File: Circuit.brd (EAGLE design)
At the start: 99 x 72.1 mm, 115 parts, among them IC1 LM1117T-3.3-V, P1 RASPI-P1RASPI_REV2_P1, P5 RASPI_P5

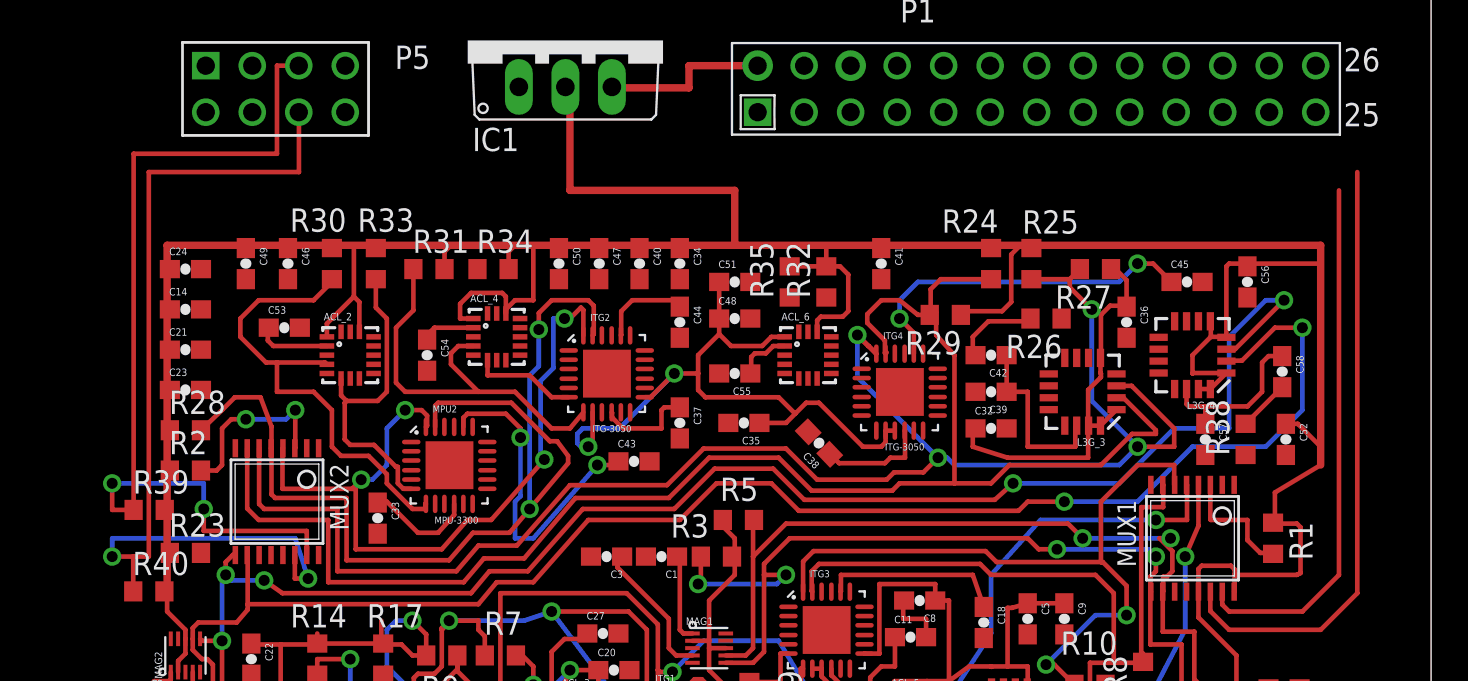
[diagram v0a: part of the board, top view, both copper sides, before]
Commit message: Rearranging buses
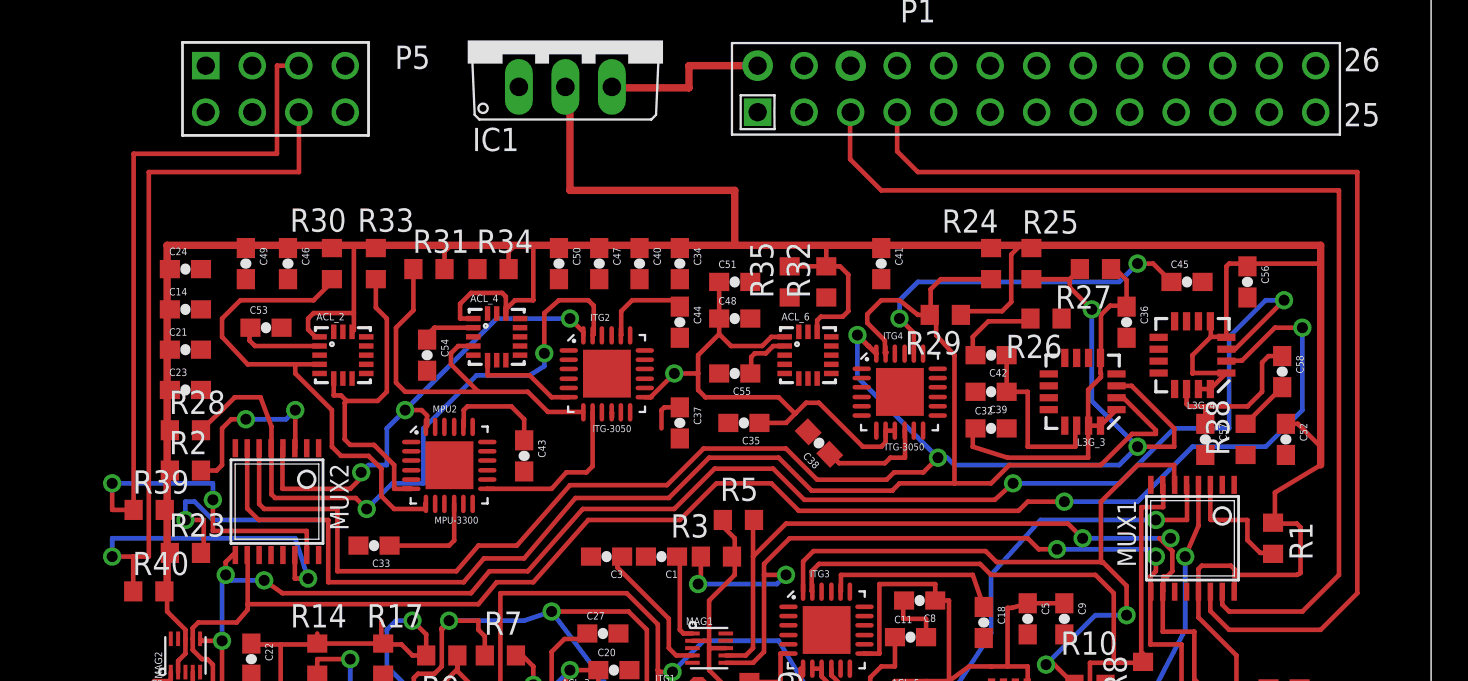
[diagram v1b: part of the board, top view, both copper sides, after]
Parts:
- moved C43 6.01 mm to (49.5, 28.5), turned to 270 degrees
- moved C33 1.51 mm to (41.3, 23.6), turned to 180 degrees
- moved C53 1.00 mm to (35.4, 35.5)
- moved ACL_2 0.40 mm to (39.6, 34.0)
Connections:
- removed net I1_INT: ITG1.12
- removed net I2_INT: ITG2.12
- removed net I3_INT: ITG3.12
- removed net I4_INT: ITG4.12
- removed net M2_INT: MPU1.12, MPU2.12
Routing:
- net SDA1: track 29.1 -> 59.1 mm
- net CLK1: track 33.3 -> 61.1 mm
- net B2_SC0: track 57.7 -> 37.2 mm
- net N$6: track 18.0 -> 5.75 mm, vias 2 -> 0
- net B2_SD0: track 41.4 -> 38.0 mm
- net N$20: track 5.30 -> 2.35 mm
- net M2_AUXSDA: track 17.6 -> 18.6 mm
- net I2_AUXCLK: track 22.4 -> 21.6 mm
- net N$5: track 4.07 -> 4.67 mm
- net +3V3: track 586.0 -> 586.5 mm, vias 5 -> 4
- net M2_AUXCLK: track 26.5 -> 27.0 mm

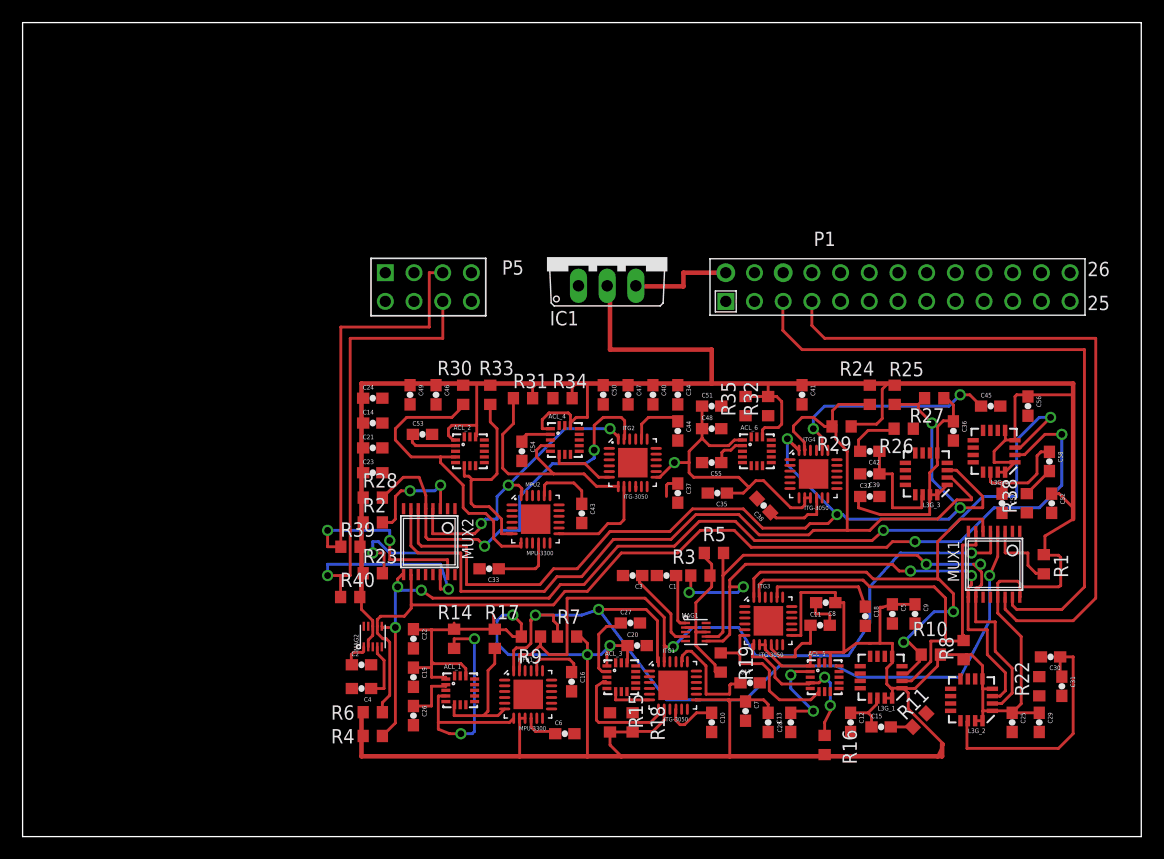
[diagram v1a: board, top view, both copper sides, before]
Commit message: Addressing DRC issues
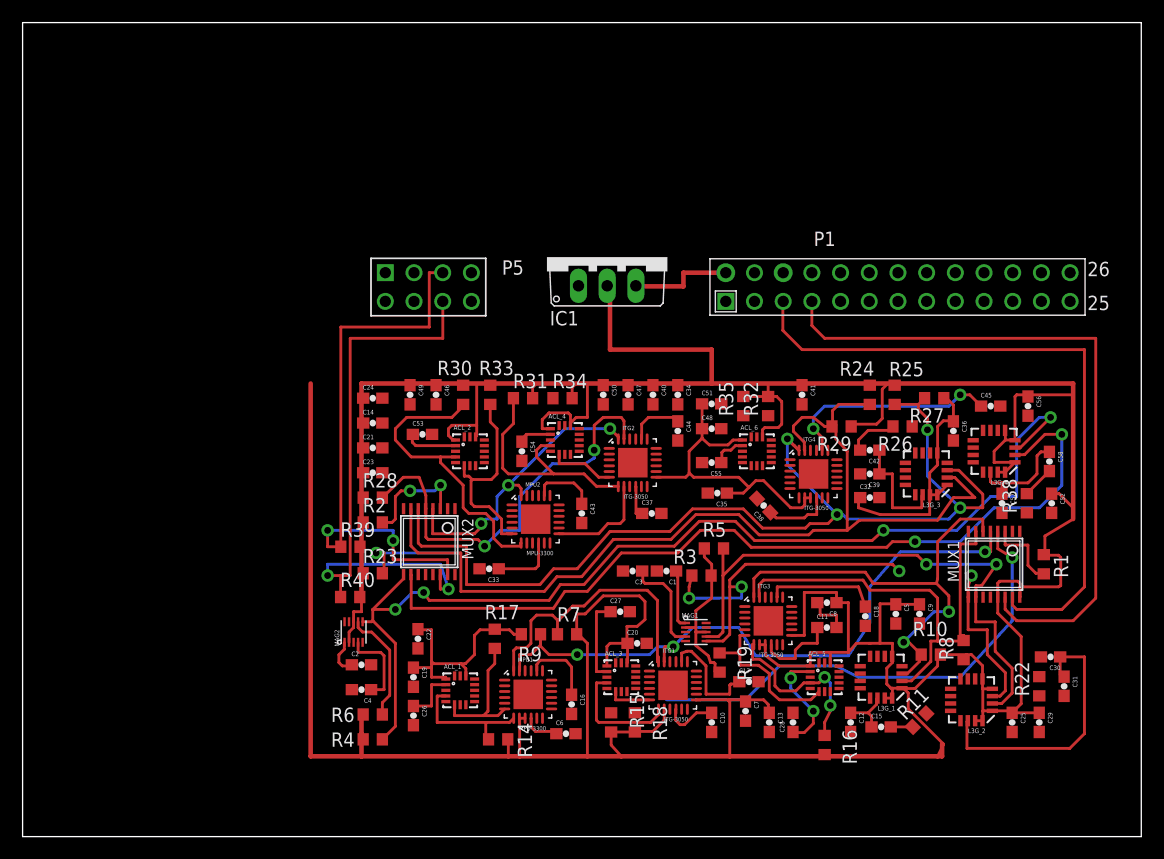
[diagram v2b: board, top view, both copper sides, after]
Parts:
- moved R14 9.72 mm to (42.1, 8.50), turned to 0 degrees
- moved C37 2.92 mm to (55.7, 28.5), turned to 0 degrees
- moved C16 2.00 mm to (48.6, 11.6)
- moved MAG2 1.75 mm to (29.3, 18.0)
- moved C27 1.35 mm to (52.9, 19.8)
- moved C11 0.63 mm to (71.2, 18.4)
- moved C9 0.40 mm to (79.4, 19.6)
- moved C1 0.40 mm to (57.0, 23.4)
- moved C22 0.40 mm to (35.0, 17.4)
- moved C3 0.40 mm to (54.0, 23.4)
- moved R5 0.40 mm to (61.2, 25.4)
- moved R4 0.30 mm to (31.0, 8.50)
- moved C5 0.30 mm to (77.3, 19.6)
- moved R26 0.22 mm to (77.9, 36.2)
- moved C28 0.20 mm to (68.2, 10.0)
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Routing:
- net +3V3: track 586.5 -> 623.3 mm, vias 4 -> 0
- net M1_AUXCLK: track 24.6 -> 11.8 mm, vias 2 -> 0
- net B1_SD0: track 76.7 -> 68.8 mm, vias 3 -> 1
- net B1_SC0: track 65.2 -> 58.3 mm, vias 2 -> 3
- net B1_SD2: track 51.4 -> 46.2 mm
- net B2_SD2: track 89.9 -> 94.5 mm, vias 5 -> 4
- net N$49: track 5.09 -> 7.46 mm
- net B2_SC2: track 88.4 -> 86.2 mm
- net N$36: track 22.2 -> 24.4 mm
- net B2_SD0: track 38.0 -> 35.9 mm
- net N$9: track 6.21 -> 7.90 mm
- net B1_SC2: track 49.7 -> 51.1 mm
- net N$1: track 5.14 -> 6.55 mm
- net N$23: track 8.05 -> 9.31 mm
- net N$53: track 7.72 -> 8.85 mm
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
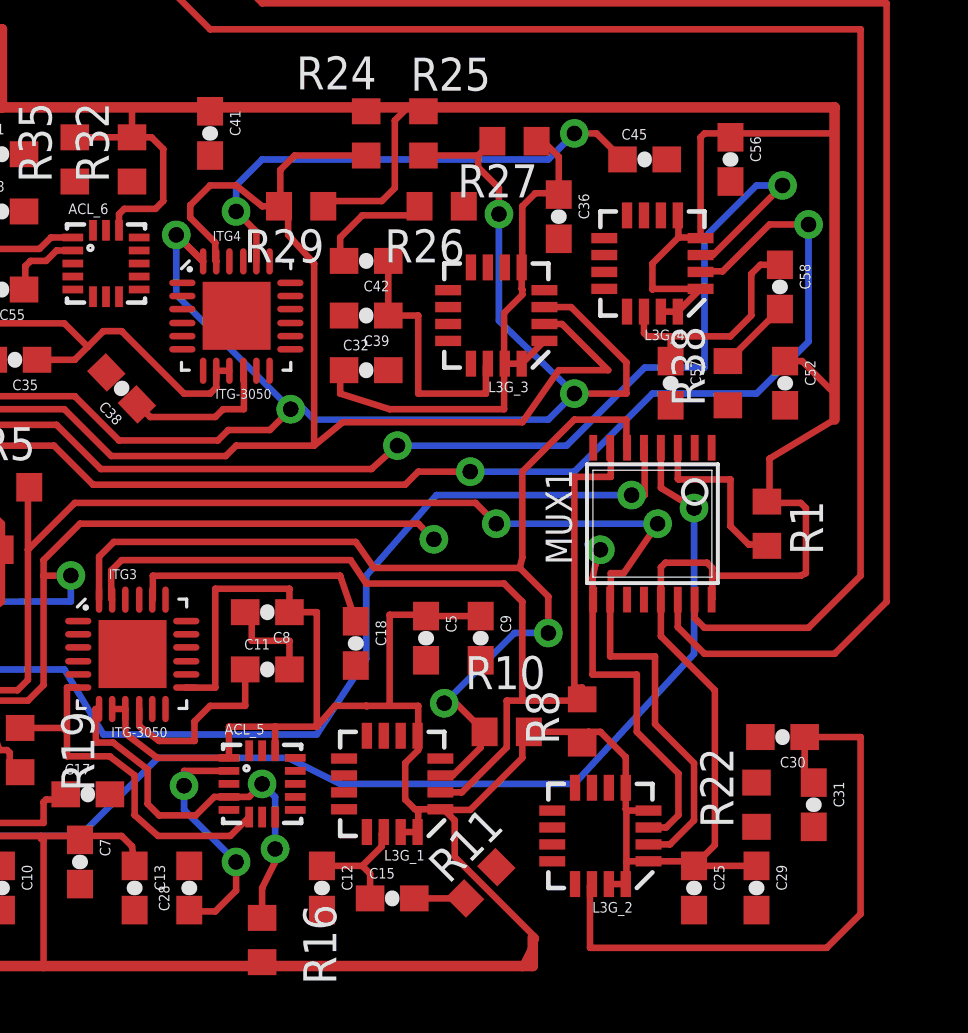
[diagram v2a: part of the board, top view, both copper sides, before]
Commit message: All simple design rule checks performed
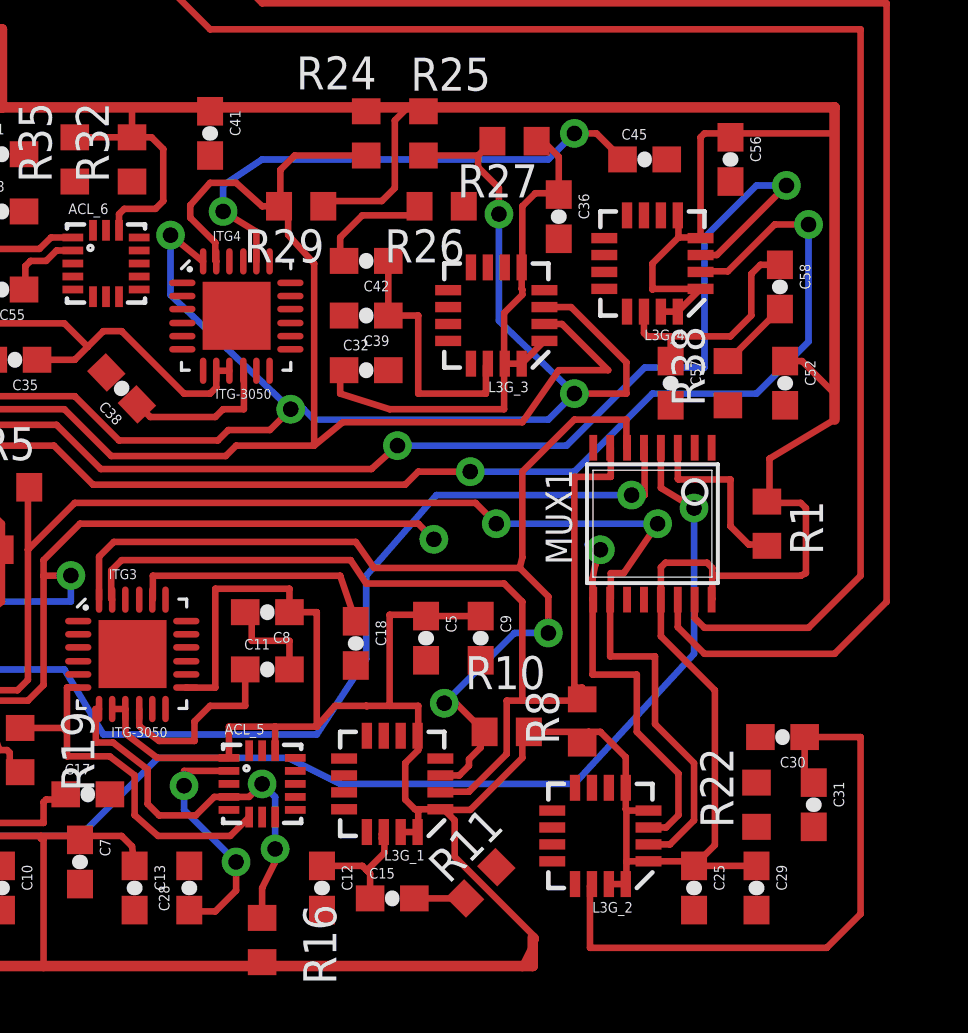
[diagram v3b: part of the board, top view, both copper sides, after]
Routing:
- net B2_SD1: track 91.5 -> 90.4 mm
- net N$35: track 19.3 -> 20.1 mm
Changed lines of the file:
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@@
 <setting verticaltext="up"/>
 </settings>
-<grid distance="1" unitdist="mm" unit="mm" style="lines" multiple="1" display="yes" altdistance="0.01" altunitdist="mm" altunit="mm"/>
+<grid distance="1" unitdist="mm" unit="mm" style="lines" multiple="1" display="yes" altdistance="0.05" altunitdist="mm" altunit="mm"/>
 <layers>
 <layer number="1" name="Top" color="4" fill="1" visible="yes" active="yes"/>
@@
 <contactref element="C45" pad="1"/>
 <wire x1="70.7796" y1="34.0816" x2="70.7796" y2="35.2204" width="0.254" layer="1"/>
-<wire x1="70.7796" y1="35.2204" x2="70" y2="36" width="0.254" layer="1"/>
-<via x="70" y="36" extent="1-16" drill="0.6"/>
-<wire x1="70" y1="36" x2="70" y2="37" width="0.254" layer="16"/>
-<wire x1="70" y1="37" x2="71" y2="38" width="0.254" layer="16"/>
+<wire x1="70.7796" y1="35.2204" x2="69.5" y2="36" width="0.254" layer="1"/>
+<via x="69.5" y="36" extent="1-16" drill="0.6"/>
+<wire x1="69.5" y1="36" x2="69.5" y2="37" width="0.254" layer="16"/>
+<wire x1="69.5" y1="37" x2="71" y2="38" width="0.254" layer="16"/>
 <wire x1="71" y1="38" x2="82" y2="38" width="0.254" layer="16"/>
 <wire x1="82" y1="38" x2="83" y2="39" width="0.254" layer="16"/>
@@
 <contactref element="C15" pad="1"/>
 <contactref element="L3G_1" pad="14"/>
-<wire x1="74.85" y1="10.85" x2="75.6" y2="11.6" width="0.254" layer="1"/>
-<wire x1="75.6" y1="11.6" x2="75.6" y2="12.075" width="0.254" layer="1"/>
 <wire x1="75.6" y1="12.075" x2="75.675" y2="12.15" width="0.254" layer="1"/>
 <contactref element="C12" pad="1"/>
 <wire x1="74.85" y1="10.85" x2="73.3" y2="10.85" width="0.254" layer="1"/>
 <wire x1="75.15" y1="9.6" x2="75.15" y2="10.55" width="0.254" layer="1"/>
-<wire x1="75.15" y1="10.55" x2="74.85" y2="10.85" width="0.254" layer="1"/>
+<wire x1="75.15" y1="10.55" x2="75.025" y2="10.675" width="0.254" layer="1"/>
+<wire x1="75.025" y1="10.675" x2="74.85" y2="10.85" width="0.254" layer="1"/>
+<wire x1="75.6" y1="12.075" x2="75.6" y2="11.9" width="0.254" layer="1"/>
+<wire x1="75.6" y1="11.9" x2="75.7" y2="11.8" width="0.254" layer="1"/>
+<wire x1="75.7" y1="11.8" x2="75.7" y2="11.35" width="0.254" layer="1"/>
+<wire x1="75.7" y1="11.35" x2="75.025" y2="10.675" width="0.254" layer="1"/>
 </signal>
 <signal name="N$40">
@@
 <contactref element="R10" pad="2"/>
 <contactref element="L3G_1" pad="3"/>
-<wire x1="77.85" y1="14.325" x2="78.325" y2="14.325" width="0.254" layer="1"/>
-<wire x1="78.325" y1="14.325" x2="79.4" y2="15.4" width="0.254" layer="1"/>
+<wire x1="77.85" y1="14.325" x2="78.575" y2="14.325" width="0.254" layer="1"/>
 <wire x1="79.4" y1="15.4" x2="79.4" y2="16.05" width="0.254" layer="1"/>
 <wire x1="79.4" y1="16.05" x2="79.55" y2="16" width="0.254" layer="1"/>
@@
 <wire x1="83" y1="28" x2="81" y2="26" width="0.254" layer="1"/>
 <wire x1="81" y1="26" x2="81" y2="22.7" width="0.254" layer="1"/>
+<wire x1="78.575" y1="14.325" x2="78.95" y2="14.7" width="0.254" layer="1"/>
+<wire x1="78.95" y1="14.7" x2="78.95" y2="14.95" width="0.254" layer="1"/>
+<wire x1="78.95" y1="14.95" x2="79.4" y2="15.4" width="0.254" layer="1"/>
 </signal>
 <signal name="B1_SC1">
@@
 <contactref element="L3G_1" pad="2"/>
 <contactref element="R8" pad="2"/>
-<wire x1="77.85" y1="13.675" x2="78.675" y2="13.675" width="0.254" layer="1"/>
-<wire x1="78.675" y1="13.675" x2="80.4" y2="15.4" width="0.254" layer="1"/>
 <wire x1="65.2" y1="21.1195" x2="65.2379" y2="21.0816" width="0.254" layer="1"/>
-<wire x1="80.4" y1="15.4" x2="80.4" y2="17.2" width="0.254" layer="1"/>
+<wire x1="80.4" y1="15.15" x2="80.4" y2="17.2" width="0.254" layer="1"/>
 <wire x1="80.4" y1="17.2" x2="81" y2="17.2" width="0.254" layer="1"/>
 <wire x1="81" y1="17.2" x2="81" y2="21" width="0.254" layer="1"/>
@@
 <wire x1="83" y1="17.7" x2="83.3" y2="17.7" width="0.254" layer="1"/>
 <wire x1="83.3" y1="17.7" x2="83.3" y2="17.25" width="0.254" layer="1"/>
+<wire x1="80.4" y1="15.15" x2="78.95" y2="13.7" width="0.254" layer="1"/>
+<wire x1="78.95" y1="13.7" x2="77.875" y2="13.7" width="0.254" layer="1"/>
+<wire x1="77.875" y1="13.7" x2="77.85" y2="13.675" width="0.254" layer="1"/>
 </signal>
 <signal name="B1_SC2">
@@
 <wire x1="57.3" y1="26.9" x2="59.3" y2="28.9" width="0.254" layer="1"/>
 <wire x1="59.3" y1="28.9" x2="63.8" y2="28.9" width="0.254" layer="1"/>
-<wire x1="67.7333" y1="35.0667" x2="68.3" y2="34.5" width="0.254" layer="1"/>
-<wire x1="68.3" y1="34.5" x2="68.3149" y2="34.5" width="0.254" layer="1"/>
-<wire x1="68.3149" y1="34.5" x2="68.7333" y2="34.0816" width="0.254" layer="1"/>
+<wire x1="67.7333" y1="35.0667" x2="68.3" y2="34.5" width="0" layer="19" extent="1-16"/>
+<wire x1="68.3" y1="34.5" x2="68.3149" y2="34.5" width="0" layer="19" extent="1-16"/>
+<wire x1="68.3149" y1="34.5" x2="68.7333" y2="34.0816" width="0" layer="19" extent="1-16"/>
 <wire x1="63.8" y1="28.9" x2="65.5" y2="27.2" width="0.254" layer="1"/>
 <wire x1="65.5" y1="27.2" x2="69.3" y2="27.2" width="0.254" layer="1"/>
@@
 <wire x1="82" y1="28" x2="83" y2="29" width="0.254" layer="16"/>
 <wire x1="68.7333" y1="34.0816" x2="68.7184" y2="34.0816" width="0.254" layer="1"/>
-<wire x1="68.7184" y1="34.0816" x2="67.7" y2="35.1" width="0.254" layer="1"/>
-<via x="67.7" y="35.1" extent="1-16" drill="0.6"/>
-<wire x1="67.7" y1="35.1" x2="67.7" y2="32.8" width="0.254" layer="16"/>
-<wire x1="67.7" y1="32.8" x2="72.1" y2="28.4" width="0.254" layer="16"/>
+<wire x1="68.7184" y1="34.0816" x2="67.48" y2="35.09" width="0.254" layer="1"/>
+<via x="67.48" y="35.09" extent="1-16" drill="0.6"/>
+<wire x1="67.48" y1="35.09" x2="67.48" y2="32.79" width="0.254" layer="16"/>
+<wire x1="67.48" y1="32.79" x2="72.1" y2="28.4" width="0.254" layer="16"/>
 <wire x1="77.2" y1="38.15" x2="79.3" y2="38.15" width="0.254" layer="1"/>
 <wire x1="79.3" y1="38.15" x2="79.85" y2="38.7" width="0.254" layer="1"/>
@@
 <contactref element="L3G_3" pad="2"/>
 <contactref element="R29" pad="2"/>
-<wire x1="68.2379" y1="36.2379" x2="69" y2="37" width="0.254" layer="1"/>
+<wire x1="68.2379" y1="36.2379" x2="69" y2="37.1" width="0.254" layer="1"/>
 <wire x1="68.2379" y1="36.2379" x2="68.2379" y2="35.7621" width="0.254" layer="1"/>
 <wire x1="69.2" y1="34.1437" x2="69.2379" y2="34.0816" width="0.254" layer="1"/>
@@
 <wire x1="72" y1="35.1" x2="72" y2="36.35" width="0.254" layer="1"/>
 <wire x1="72" y1="36.35" x2="71.65" y2="36.2" width="0.254" layer="1"/>
-<wire x1="69" y1="37" x2="70" y2="37" width="0.254" layer="1"/>
-<wire x1="70" y1="37" x2="71" y2="36.2" width="0.254" layer="1"/>
+<wire x1="69" y1="37.1" x2="70" y2="37.1" width="0.254" layer="1"/>
+<wire x1="70" y1="37.1" x2="71" y2="36.2" width="0.254" layer="1"/>
 <wire x1="71" y1="36.2" x2="71.65" y2="36.2" width="0.254" layer="1"/>
 <wire x1="75" y1="38.15" x2="72.25" y2="38.15" width="0.254" layer="1"/>
@@
 <wire x1="92" y1="31" x2="92" y2="35.5" width="0.254" layer="16"/>
 <via x="92" y="35.5" extent="1-16" drill="0.6"/>
-<wire x1="92" y1="35.5" x2="90.5" y2="35.5" width="0.254" layer="1"/>
-<wire x1="90.5" y1="35.5" x2="88.7" y2="33.7" width="0.254" layer="1"/>
-<wire x1="88.7" y1="33.7" x2="87.875" y2="33.7" width="0.254" layer="1"/>
+<wire x1="92" y1="35.5" x2="90.7" y2="35.5" width="0.254" layer="1"/>
+<wire x1="90.7" y1="35.5" x2="88.9" y2="33.7" width="0.254" layer="1"/>
+<wire x1="88.9" y1="33.7" x2="87.875" y2="33.7" width="0.254" layer="1"/>
 <wire x1="87.875" y1="33.7" x2="87.85" y2="33.675" width="0.254" layer="1"/>
 <wire x1="30.1" y1="18" x2="29.7" y2="18.4" width="0.254" layer="1"/>
@@
 <contactref element="MAG2" pad="6"/>
 <contactref element="R4" pad="1"/>
-<wire x1="87.85" y1="34.325" x2="88.325" y2="34.325" width="0.254" layer="1"/>
-<wire x1="88.325" y1="34.325" x2="91" y2="37" width="0.254" layer="1"/>
-<via x="91" y="37" extent="1-16" drill="0.6"/>
-<wire x1="91" y1="37" x2="90" y2="37" width="0.254" layer="16"/>
+<wire x1="87.85" y1="34.325" x2="88.475" y2="34.325" width="0.254" layer="1"/>
+<wire x1="88.475" y1="34.325" x2="91.15" y2="37" width="0.254" layer="1"/>
+<via x="91.15" y="37" extent="1-16" drill="0.6"/>
+<wire x1="91.15" y1="37" x2="90" y2="37" width="0.254" layer="16"/>
 <wire x1="90" y1="37" x2="88" y2="35" width="0.254" layer="16"/>
 <wire x1="88" y1="35" x2="88" y2="30" width="0.254" layer="16"/>
